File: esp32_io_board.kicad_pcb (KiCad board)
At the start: 2 copper layers, 59 parts, among them J1 USB_B_Micro, J10 Conn_02x04_Counter_Clockwise, J11 Conn_01x02, J12 Conn_01x02, J13 Conn_01x02, J14 Conn_01x02, J15 Conn_01x02, J16 Conn_01x02, J17 Conn_01x02, J18 Conn_01x02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

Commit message: redesign
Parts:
- D2: footprint Diode_SMD:D_SOD-323F -> Diode_SMD:D_SOD-123F
- D7: footprint LED_SMD:LED_RGB_5050-6 -> LED_SMD:LED_0603_1608Metric
- moved C8 88.5 mm to (171.7, 88.6)
- moved R6 86.1 mm to (175.5, 88.6), turned to 180 degrees
- moved C3 86.1 mm to (169.2, 95.5), turned to 180 degrees
- moved J3 80.6 mm to (171.4, 91.9), turned to 90 degrees
- moved C5 79.2 mm to (169.2, 103.1)
- moved C6 78.6 mm to (175.5, 103.1)
- moved C4 77.8 mm to (175.5, 95.5), turned to 180 degrees
- moved SW1 72.7 mm to (163.8, 90.7), turned to 270 degrees
- moved J11 70.7 mm to (180.6, 126.7), turned to 180 degrees
- moved J18 69.0 mm to (188.5, 116.1)
- moved U2 67.8 mm to (172.0, 99.3)
- moved D3 67.4 mm to (177.8, 113.0), turned to 180 degrees
- moved D6 66.1 mm to (168.9, 113.0), turned to 180 degrees
- moved R10 65.7 mm to (194.8, 122.2)
- moved J5 65.3 mm to (178.3, 119.1), turned to 270 degrees
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
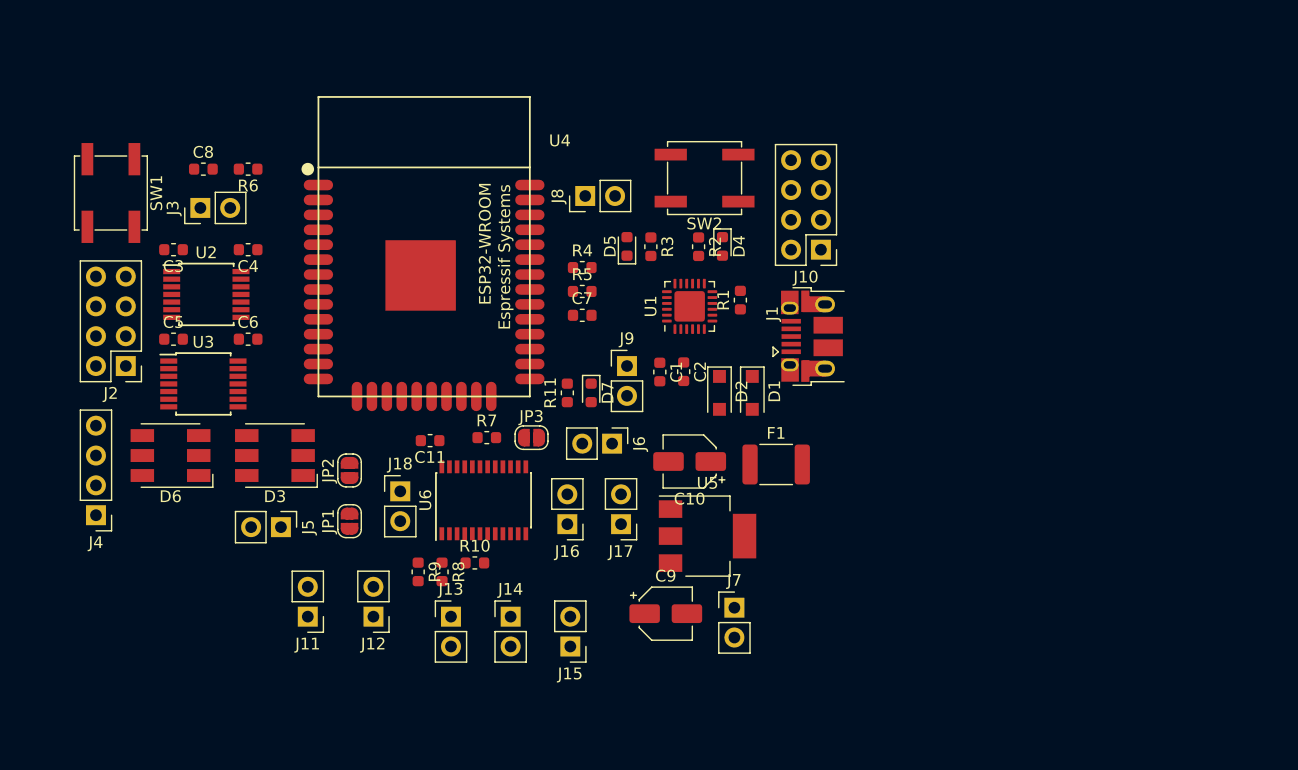
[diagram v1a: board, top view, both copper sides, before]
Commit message: raspberry pi integration
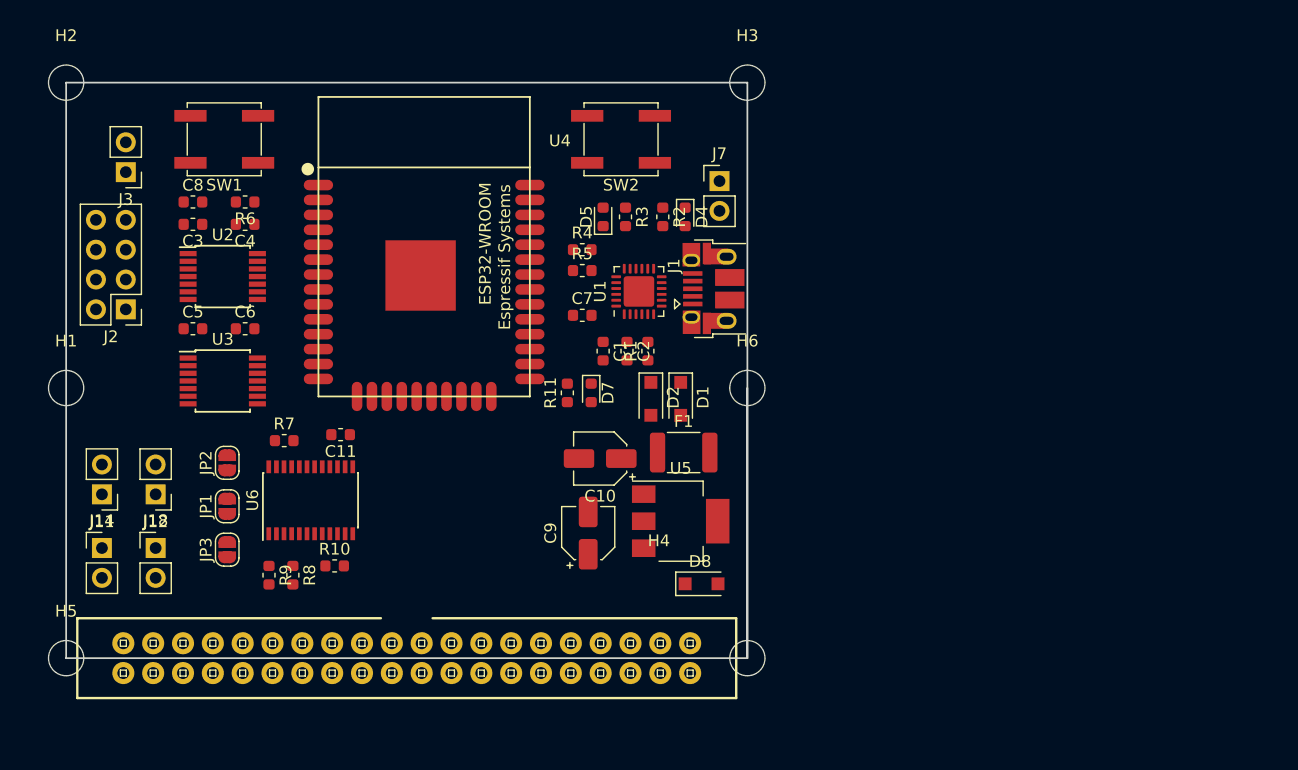
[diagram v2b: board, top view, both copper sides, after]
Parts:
- removed D3, D6: LED_RGB, LED_SMD:LED_RGB_5050-6
- removed J10: Conn_02x04_Counter_Clockwise, Connector_PinHeader_2.54mm:PinHeader_2x04_P2.54mm_Vertical
- removed J13, J15, J16, J17, J6, J8, J9: Conn_01x02, Connector_PinHeader_2.54mm:PinHeader_1x02_P2.54mm_Vertical
- removed J4: Conn_01x04, Connector_PinHeader_2.54mm:PinHeader_1x04_P2.54mm_Vertical
- added D8: D, Diode_SMD:D_SOD-123F, F.Cu at (214.1, 124.0)
- added H1: MountingHole, MountingHole:MountingHole_3mm, F.Cu at (160.0, 107.3)
- added H2: MountingHole, MountingHole:MountingHole_3mm, F.Cu at (160.0, 81.3)
- added H3: MountingHole, MountingHole:MountingHole_3mm, F.Cu at (218.0, 81.3)
- added H4: MountingHole, MountingHole:MountingHole_3mm, F.Cu at (218.0, 130.3)
- added H5: MountingHole, MountingHole:MountingHole_3mm, F.Cu at (160.0, 130.3)
- added H6: MountingHole, MountingHole:MountingHole_3mm, F.Cu at (218.0, 107.3)
- J5: value i2c -> RASPBERRYPI-40-PIN-GPIO; footprint Connector_PinHeader_2.54mm:PinHeader_1x02_P2.54mm_Vertical -> SparkFun-Boards:2X20-SHROUDED
- moved J7 36.3 mm to (215.6, 89.7)
- moved J14 35.3 mm to (163.1, 120.9)
- moved JP3 27.6 mm to (173.7, 121.0), turned to 90 degrees
- moved J18 21.4 mm to (167.6, 120.9)
- moved J12 21.3 mm to (167.6, 116.3)
- moved J11 20.4 mm to (163.1, 116.3)
- moved R7 17.2 mm to (178.6, 111.8)
- moved J5 15.5 mm to (189.0, 130.3)
- moved U6 14.7 mm to (180.8, 116.8)
- moved R8 12.7 mm to (179.3, 123.2)
- moved R9 12.7 mm to (177.3, 123.2)
- moved R10 11.9 mm to (182.9, 122.4)
- moved SW1 10.7 mm to (173.5, 86.1), turned to 180 degrees
- moved JP1 10.5 mm to (173.7, 117.3)
- moved JP2 10.4 mm to (173.7, 113.7)
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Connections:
- J5 pad 1: Net-(J5-Pad1) -> Net-(D8-Pad1)
- U4 pad 17: Net-(J5-Pad2) -> Net-(U4-Pad17)
- U4 pad 18: Net-(J5-Pad1) -> Net-(U4-Pad18)
- U4 pad 23: Net-(J6-Pad2) -> Net-(U4-Pad23)
- U4 pad 24: Net-(J6-Pad1) -> Net-(U4-Pad24)
- U4 pad 27: Net-(J9-Pad2) -> /rx
- U4 pad 28: Net-(J9-Pad1) -> /tx
- U4 pad 29: Net-(J10-Pad4) -> /cs
- U4 pad 30: Net-(J10-Pad3) -> /clk
- U4 pad 31: Net-(J10-Pad2) -> /miso
- U4 pad 33: Net-(J8-Pad2) -> /sda0
- U4 pad 36: Net-(J8-Pad1) -> /scl0
- U4 pad 37: Net-(J10-Pad1) -> /mosi
- U6 pad 22: Net-(U4-Pad22) -> Net-(U4-Pad24)
- U6 pad 23: Net-(U4-Pad21) -> Net-(U4-Pad23)
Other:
- board outline added: 58 x 49 mm

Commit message: layout
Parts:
- removed J18: Conn_01x02, Connector_PinHeader_2.54mm:PinHeader_1x02_P2.54mm_Vertical
- added J13: Conn_01x02, Connector_PinHeader_2.54mm:PinHeader_1x02_P2.54mm_Vertical, F.Cu at (167.6, 120.9)
- added J4: Conn_01x02, Connector_PinHeader_2.54mm:PinHeader_1x02_P2.54mm_Vertical, F.Cu at (194.3, 112.3)
- added JP4: SolderJumper_2_Open, Jumper:SolderJumper-2_P1.3mm_Open_RoundedPad1.0x1.5mm, F.Cu at (182.1, 123.7)
- added JP5: SolderJumper_2_Open, Jumper:SolderJumper-2_P1.3mm_Open_RoundedPad1.0x1.5mm, F.Cu at (174.0, 123.7)
- added JP6: SolderJumper_2_Open, Jumper:SolderJumper-2_P1.3mm_Open_RoundedPad1.0x1.5mm, F.Cu at (171.2, 123.7)
- added JP7: SolderJumper_2_Open, Jumper:SolderJumper-2_P1.3mm_Open_RoundedPad1.0x1.5mm, F.Cu at (184.9, 123.7)
- added JP8: SolderJumper_2_Open, Jumper:SolderJumper-2_P1.3mm_Open_RoundedPad1.0x1.5mm, F.Cu at (190.2, 120.4)
- added JP9: SolderJumper_2_Open, Jumper:SolderJumper-2_P1.3mm_Open_RoundedPad1.0x1.5mm, F.Cu at (186.9, 119.9)
- added R12: R_Small, Resistor_SMD:R_0603_1608Metric, F.Cu at (193.8, 117.6)
- added R13: R_Small, Resistor_SMD:R_0603_1608Metric, F.Cu at (197.1, 113.5)
- added R14: R_Small, Resistor_SMD:R_0603_1608Metric, F.Cu at (198.9, 112.5)
- added R15: R_Small, Resistor_SMD:R_0603_1608Metric, F.Cu at (193.8, 119.4)
- added R16: R_Small, Resistor_SMD:R_0603_1608Metric, F.Cu at (193.8, 121.2)
- added U7: CAT24C256, Package_SO:SOIC-8-1EP_3.9x4.9mm_P1.27mm_EP2.35x2.35mm, F.Cu at (189.0, 114.6)
- moved C1 10.3 mm to (212.3, 96.3), turned to 90 degrees
- moved JP3 10.1 mm to (174.8, 111.0), turned to 180 degrees
- moved R8 5.12 mm to (174.8, 120.9), turned to 180 degrees
- moved R9 4.81 mm to (174.8, 119.1), turned to 180 degrees
- moved R10 3.89 mm to (179.1, 121.7)
- moved R1 3.57 mm to (213.1, 103.9), turned to 180 degrees
- moved C8 1.76 mm to (171.7, 89.9)
- moved J1 1.52 mm to (216.7, 98.8)
- moved R6 1.52 mm to (175.3, 89.9)
- moved C4 1.42 mm to (176.5, 94.0)
- moved C6 1.42 mm to (176.5, 102.9)
- moved SW1 1.37 mm to (174.8, 85.6)
- moved JP1 1.27 mm to (174.8, 116.6), turned to 180 degrees
- moved JP2 1.03 mm to (174.8, 113.8), turned to 180 degrees
- moved D2 1.02 mm to (208.8, 108.2)
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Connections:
- C6 pad 1: 3.3V -> +3V3
- J5 pad 27: Net-(J5-Pad27) -> /id_sda
- J5 pad 28: Net-(J5-Pad28) -> /id_clk
- U4 pad 14: /di -> Net-(J4-Pad2)
- U4 pad 16: /ci -> Net-(J4-Pad1)
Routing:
- net +3V3: track 0.00 -> 35.3 mm, vias 0 -> 7
- net Net-(R13-Pad1): track 0.00 -> 28.5 mm, vias 0 -> 2
- net Net-(R14-Pad1): track 0.00 -> 26.3 mm, vias 0 -> 2
- net Net-(J14-Pad2): track 0.00 -> 25.8 mm, vias 0 -> 1
- net Net-(J14-Pad1): track 0.00 -> 24.2 mm, vias 0 -> 1
- net /id_clk: track 0.00 -> 22.4 mm, vias 0 -> 1
- net Net-(J11-Pad1): track 0.00 -> 21.2 mm, vias 0 -> 2
- net Net-(J11-Pad2): track 0.00 -> 20.3 mm, vias 0 -> 1
- net Net-(J3-Pad1): track 0.00 -> 20.1 mm
- net Net-(JP4-Pad2): track 0.00 -> 18.1 mm, vias 0 -> 2
- net Net-(J13-Pad2): track 0.00 -> 18.0 mm
- net Net-(J5-Pad35): track 0.00 -> 17.6 mm, vias 0 -> 1
- net Net-(J3-Pad2): track 0.00 -> 17.3 mm
- net /id_sda: track 0.00 -> 17.0 mm, vias 0 -> 1
- net Net-(J12-Pad2): track 0.00 -> 16.6 mm, vias 0 -> 1
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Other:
- board outline removed
- net class Default: via_dia 0.8 -> 0.6

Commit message: layout update
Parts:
- removed C3, C4, C5, C6: C_Small, Capacitor_SMD:C_0603_1608Metric
- removed JP5, JP6: SolderJumper_2_Open, Jumper:SolderJumper-2_P1.3mm_Open_RoundedPad1.0x1.5mm
- removed U2, U3: TXB0104PW, Package_SO:TSSOP-14_4.4x5mm_P0.65mm
- moved J4 34.6 mm to (163.2, 97.2)
- moved J7 23.5 mm to (211.5, 112.8), turned to 90 degrees
- moved F1 22.9 mm to (216.1, 90.2), turned to 270 degrees
- moved J2 10.3 mm to (173.4, 106.7), turned to 270 degrees
- moved JP3 4.40 mm to (178.4, 108.6), turned to 90 degrees
- moved R14 3.74 mm to (195.3, 113.5)
- moved R13 3.56 mm to (193.5, 113.5)
- moved J3 3.47 mm to (163.2, 91.4), turned to 180 degrees
- moved C9 1.95 mm to (206.3, 120.3)
- moved U5 1.40 mm to (213.7, 118.5)
- moved C10 0.26 mm to (205.4, 113.5)
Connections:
- J7 pad 1: +5V -> VCC
- U4 pad 10: /pin10 -> Net-(J2-Pad4)
- U4 pad 11: /pin11 -> Net-(J2-Pad3)
- U4 pad 12: /pin12 -> Net-(J2-Pad2)
- U4 pad 13: /pin13 -> Net-(J2-Pad1)
- U4 pad 6: /pin6 -> Net-(J2-Pad5)
- U4 pad 7: /pin7 -> Net-(J2-Pad6)
- U4 pad 8: /pin8 -> Net-(J2-Pad7)
- U4 pad 9: /pin9 -> Net-(J2-Pad8)
- U7 pad 1: Net-(U7-Pad1) -> GND
- U7 pad 2: Net-(U7-Pad1) -> GND
- U7 pad 3: Net-(U7-Pad1) -> GND
- U7 pad 4: Net-(U7-Pad1) -> GND
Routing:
- net GND: track 2.62 -> 55.5 mm, vias 1 -> 25
- net /mosi: track 0.00 -> 46.2 mm, vias 0 -> 1
- net /scl0: track 0.00 -> 44.1 mm, vias 0 -> 2
- net /sda0: track 0.00 -> 41.8 mm, vias 0 -> 1
- net Net-(SW2-Pad1): track 0.00 -> 37.9 mm, vias 0 -> 2
- net /cs: track 0.00 -> 37.4 mm, vias 0 -> 1
- net /miso: track 0.00 -> 36.9 mm, vias 0 -> 1
- net /clk: track 0.00 -> 36.8 mm, vias 0 -> 1
- net /tx: track 0.00 -> 34.7 mm, vias 0 -> 1
- net /rx: track 0.00 -> 32.9 mm, vias 0 -> 1
- net +3V3: track 35.3 -> 2.62 mm, vias 7 -> 1
- net Net-(J4-Pad2): track 0.00 -> 31.4 mm, vias 0 -> 1
- net Net-(J4-Pad1): track 0.00 -> 30.5 mm, vias 0 -> 1
- net /RESET: track 6.54 -> 36.0 mm, vias 0 -> 2
- net Net-(F1-Pad1): track 0.00 -> 19.7 mm, vias 0 -> 3
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
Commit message: layout design
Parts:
- moved J1 1.30 mm to (217.9, 99.1)
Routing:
- net GND: track 55.5 -> 135.6 mm, vias 25 -> 34
- net +3V3: track 2.62 -> 16.3 mm, vias 1 -> 2
- net Net-(J2-Pad5): track 21.9 -> 23.9 mm
- net Net-(JP4-Pad2): track 21.7 -> 23.3 mm
- net Net-(J2-Pad3): track 12.3 -> 13.9 mm
- net Net-(D2-Pad1): track 15.3 -> 16.7 mm
- net /mosi: track 46.2 -> 47.4 mm
- net Net-(D1-Pad1): track 13.9 -> 15.0 mm
- net Net-(J2-Pad4): track 17.4 -> 18.5 mm
- net /tx: track 34.7 -> 35.8 mm
- net /sda0: track 41.8 -> 42.9 mm
- net +5V: track 16.5 -> 17.5 mm
- net /clk: track 36.8 -> 37.7 mm
- net /rx: track 32.9 -> 33.6 mm
- net Net-(J13-Pad2): track 18.0 -> 18.6 mm, vias 0 -> 2
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- added copper zone on F.Cu, net +3V3
- added copper zone on B.Cu, net GND
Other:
- board outline added: 65 x 55.9 mm
- net class power added: clearance 0.2, trace_width 1.5, via_dia 0.6, via_drill 0.4

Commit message: pcb final layout adjustments
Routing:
- net GND: track 135.6 -> 58.8 mm, vias 34 -> 27
- net /mosi: track 47.4 -> 46.6 mm
- net +3V3: track 16.3 -> 16.8 mm
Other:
- board size 65 x 55.9 mm -> 65.1 x 56.1 mm
